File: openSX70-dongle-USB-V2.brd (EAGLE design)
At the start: 20 x 45 mm, 25 parts, among them J1 687106183722, J2 SJ-3523-SMT-TR, U1 FT232RLSSOP

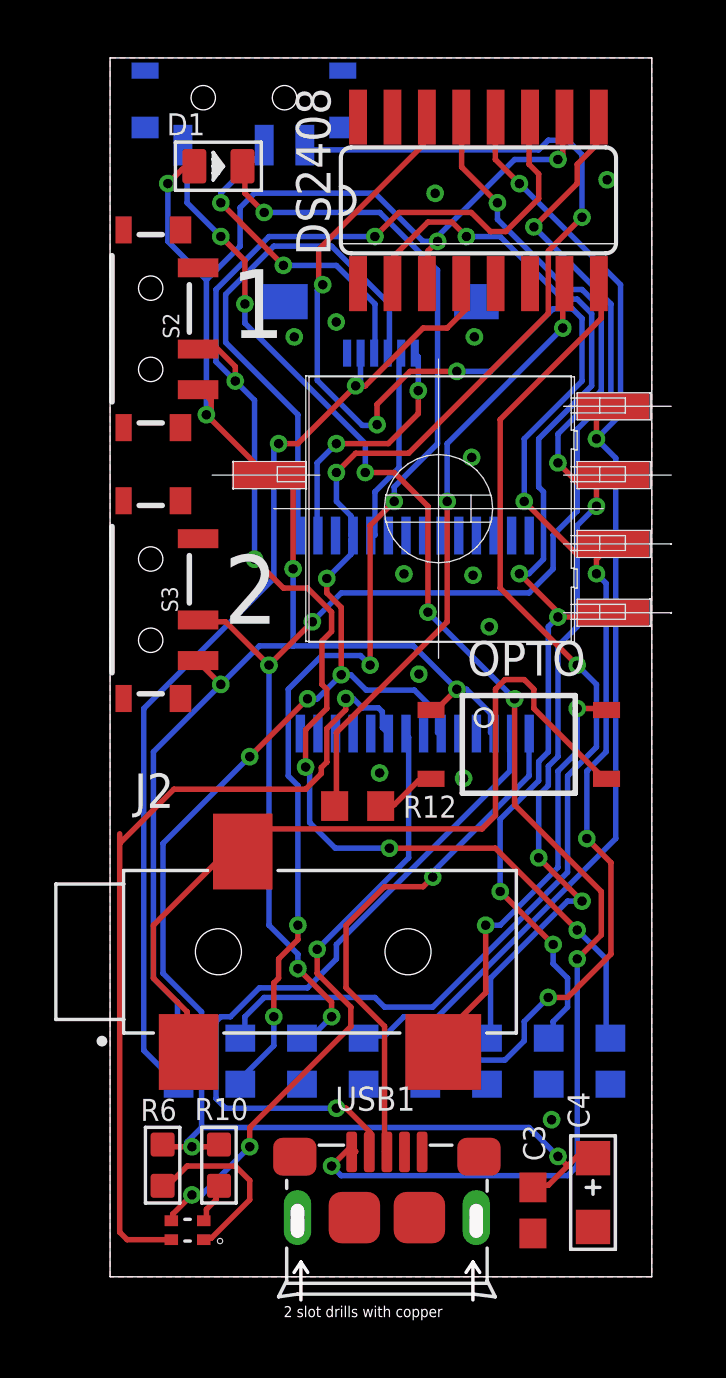
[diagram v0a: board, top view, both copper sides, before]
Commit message: fixed dual led footprint
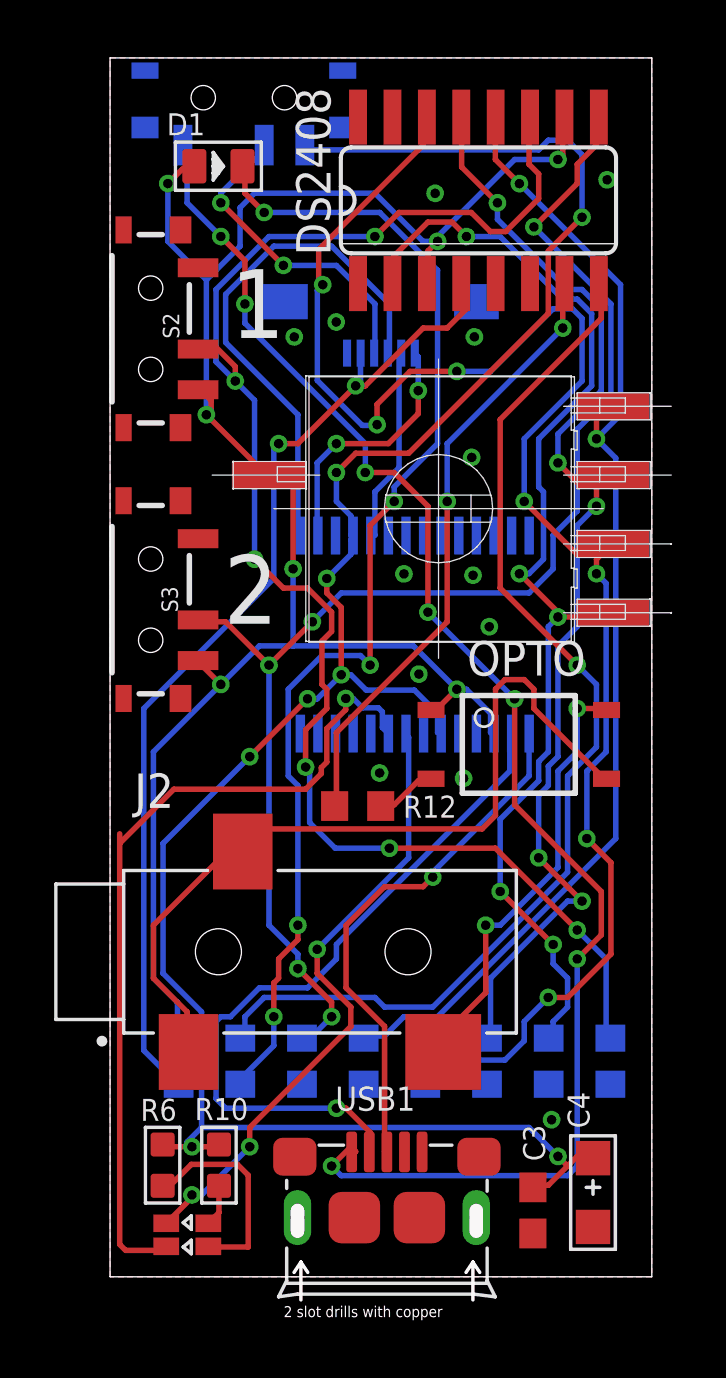
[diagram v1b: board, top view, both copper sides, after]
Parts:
- removed U$1: DUAL-LED-0603-BIS, _openSX70:LED_APHB1608SYKSURKC
- added U$5: DUOLED-PROPER-LTST-C195KGJRKT, _openSX70:LTST-BILED-15X16
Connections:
- net N$14: now also R6.1, U$5.P$1; no longer R10.1, U$1.3
- net N$9: now also R10.1, U$5.P$2; no longer R6.1, U$1.1
- net RXLED: now also U$5.P$4; no longer U$1.4
- net TXLED: now also U$5.P$3; no longer U$1.2
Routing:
- net N$14: track 1.52 -> 7.79 mm
- net N$9: track 6.96 -> 1.55 mm
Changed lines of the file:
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@@
 <attribute name="VALUE" x="7.347140625" y="9.23" size="1.27" layer="28" rot="MR270"/>
 </element>
-<element name="S1" library="SparkFun-Switches" library_urn="urn:adsk.eagle:library:535" package="SWITCH_SPST_SMD_A" package3d_urn="urn:adsk.eagle:package:40179/1" value="" x="4.94" y="43.53" rot="MR0">
+<element name="S1" library="SparkFun-Switches" package="SWITCH_SPST_SMD_A" value="" x="4.94" y="43.53" rot="MR0">
 <attribute name="NAME" x="4.878" y="43.033" size="0.6096" layer="26" font="vector" ratio="20" rot="MR180" align="bottom-center"/>
 <attribute name="PROD_ID" value="SWCH-10651" x="-23" y="-6" size="1.778" layer="28" rot="MR0" display="off"/>
@@
 <attribute name="VALUE" x="24.516" y="18.16" size="1.778" layer="27" ratio="10" rot="R90"/>
 </element>
-<element name="U$1" library="_openSX70" package="LED_APHB1608SYKSURKC" value="DUAL-LED-0603-BIS" x="2.86" y="1.72" rot="R180">
-<attribute name="NAME" x="4.71323125" y="0.81843125" size="0.81421875" layer="31" rot="R180"/>
-<attribute name="VALUE" x="4.863" y="3.42255" size="0.814021875" layer="27" rot="R180"/>
-</element>
 <element name="U1" library="SparkFun" package="SSOP28DB" value="FT232RLSSOP" x="11.25" y="23.71" rot="MR180">
 <attribute name="NAME" x="7.44" y="22.44" size="0.4064" layer="26" rot="MR180"/>
@@
 <attribute name="VALUE" x="5.14" y="0.415" size="0.889" layer="27" ratio="11" rot="R90"/>
 </element>
-<element name="S2" library="SparkFun-Switches" library_urn="urn:adsk.eagle:library:535" package="SWITCH_SPST_SMD_A" package3d_urn="urn:adsk.eagle:package:40179/1" value="" x="1.5" y="35" rot="R90">
+<element name="S2" library="SparkFun-Switches" package="SWITCH_SPST_SMD_A" value="" x="1.5" y="35" rot="R90">
 <attribute name="NAME" x="1.947" y="35.112" size="0.6096" layer="25" font="vector" ratio="20" rot="R270" align="bottom-center"/>
 <attribute name="PROD_ID" value="SWCH-10651" x="1.5" y="35" size="1.778" layer="27" rot="R90" display="off"/>
@@
 <attribute name="VALUE" x="0.103" y="35" size="0.6096" layer="27" font="vector" ratio="20" rot="R270" align="top-center"/>
 </element>
-<element name="S3" library="SparkFun-Switches" library_urn="urn:adsk.eagle:library:535" package="SWITCH_SPST_SMD_A" package3d_urn="urn:adsk.eagle:package:40179/1" value="" x="1.5" y="25" rot="R90">
+<element name="S3" library="SparkFun-Switches" package="SWITCH_SPST_SMD_A" value="" x="1.5" y="25" rot="R90">
 <attribute name="NAME" x="1.897" y="25.012" size="0.6096" layer="25" font="vector" ratio="20" rot="R270" align="bottom-center"/>
 <attribute name="PROD_ID" value="SWCH-10651" x="1.5" y="25" size="1.778" layer="27" rot="R90" display="off"/>
@@
 <attribute name="NAME" x="2.095" y="42.143" size="0.8128" layer="25" font="vector" ratio="11"/>
 <attribute name="VALUE" x="2.303" y="39.3125" size="0.635" layer="27" ratio="10"/>
+</element>
+<element name="U$5" library="_openSX70" package="LTST-BILED-15X16" value="DUOLED-PROPER-LTST-C195KGJRKT" x="2.85" y="1.55" rot="R270">
+<attribute name="AVAILABILITY" value="Unavailable" x="2.85" y="1.55" size="1.778" layer="27" rot="R270" display="off"/>
+<attribute name="DESCRIPTION" value=" Green/Red 130° Water Clear 35/25 mcd 2 V 0605 Surface Mount Bi-Color LED " x="2.85" y="1.55" size="1.778" layer="27" rot="R270" display="off"/>
+<attribute name="MF" value="Lite-On Inc." x="2.85" y="1.55" size="1.778" layer="27" rot="R270" display="off"/>
+<attribute name="MP" value="LTST-C195KGJRKT" x="2.85" y="1.55" size="1.778" layer="27" rot="R270" display="off"/>
+<attribute name="PACKAGE" value="0606 Lite-On" x="2.85" y="1.55" size="1.778" layer="27" rot="R270" display="off"/>
+<attribute name="PRICE" value="None" x="2.85" y="1.55" size="1.778" layer="27" rot="R270" display="off"/>
 </element>
 </elements>
@@
 <signal name="TXLED">
 <contactref element="U1" pad="23"/>
-<contactref element="U$1" pad="2"/>
-<wire x1="2.26" y1="1.37" x2="0.63" y2="1.37" width="0.2032" layer="1"/>
-<wire x1="0.63" y1="1.37" x2="0.3556" y2="1.6444" width="0.2032" layer="1"/>
-<wire x1="0.3556" y1="1.6444" x2="0.3556" y2="16" width="0.2032" layer="1"/>
+<wire x1="0.575" y1="0.975" x2="0.3556" y2="1.1944" width="0.2032" layer="1"/>
+<wire x1="0.3556" y1="1.1944" x2="0.3556" y2="16" width="0.2032" layer="1"/>
 <wire x1="0.3556" y1="16" x2="0.3556" y2="16.3556" width="0.2032" layer="1"/>
 <wire x1="10.275" y1="20.054" x2="10.053" y2="20.276" width="0.2032" layer="16"/>
@@
 <wire x1="8.7" y1="21.35" x2="8.7" y2="20.9377" width="0.2032" layer="1"/>
 <wire x1="8.7" y1="20.9377" x2="8.001" y2="20.2387" width="0.2032" layer="1"/>
-<wire x1="8.001" y1="19.001" x2="8" y2="19" width="0.2032" layer="1"/>
 <wire x1="8.001" y1="20.2387" x2="8.001" y2="19.001" width="0.2032" layer="1"/>
 <wire x1="2.3556" y1="18" x2="0.3556" y2="16" width="0.2032" layer="1"/>
-<wire x1="8" y1="19" x2="7.799" y2="18.799" width="0.2032" layer="1"/>
+<wire x1="8.001" y1="19.001" x2="7.799" y2="18.799" width="0.2032" layer="1"/>
 <wire x1="7.799" y1="18.799" x2="7.799" y2="18.578175" width="0.2032" layer="1"/>
 <wire x1="7.799" y1="18.578175" x2="7.220825" y2="18" width="0.2032" layer="1"/>
 <wire x1="7.220825" y1="18" x2="2.3556" y2="18" width="0.2032" layer="1"/>
+<contactref element="U$5" pad="P$3"/>
+<wire x1="1.9242" y1="0.975" x2="0.575" y2="0.975" width="0.2032" layer="1"/>
+<wire x1="2.0742" y1="1.125" x2="1.9242" y2="0.975" width="0.2032" layer="1"/>
 </signal>
 <signal name="RXLED">
 <contactref element="U1" pad="22"/>
-<contactref element="U$1" pad="4"/>
-<wire x1="2.3114" y1="2.3114" x2="2.3114" y2="2.1336" width="0.2032" layer="1"/>
-<wire x1="3.0226" y1="3.0226" x2="2.3114" y2="2.3114" width="0.2032" layer="1"/>
 <wire x1="3.3782" y1="3.0226" x2="3.0226" y2="3.0226" width="0.2032" layer="16"/>
 <wire x1="5.1562" y1="4.8006" x2="3.3782" y2="3.0226" width="0.2032" layer="16"/>
@@
 <wire x1="11.0236" y1="15.4686" x2="7.6454" y2="12.0904" width="0.2032" layer="16"/>
 <wire x1="11.0236" y1="19.9136" x2="11.0236" y2="15.4686" width="0.2032" layer="16"/>
-<wire x1="2.3114" y1="2.1336" x2="2.26" y2="2.07" width="0.2032" layer="1"/>
 <wire x1="11.0236" y1="19.9136" x2="10.925" y2="20.054" width="0.2032" layer="16"/>
 <via x="3.0226" y="3.0226" extent="1-16" drill="0.35"/>
 <via x="5.1562" y="4.8006" extent="1-16" drill="0.35"/>
 <via x="7.6454" y="12.0904" extent="1-16" drill="0.35"/>
+<contactref element="U$5" pad="P$4"/>
+<wire x1="3.0226" y1="3.0226" x2="3.0226" y2="2.9234" width="0.2032" layer="1"/>
+<wire x1="3.0226" y1="2.9234" x2="2.0742" y2="1.975" width="0.2032" layer="1"/>
 </signal>
 <signal name="TXO">
@@
 <via x="6.4008" y="37.338" extent="1-16" drill="0.35"/>
 <via x="4.0894" y="39.6494" extent="1-16" drill="0.35"/>
-</signal>
-<signal name="N$9">
-<contactref element="R6" pad="1"/>
-<contactref element="U$1" pad="1"/>
-<wire x1="3.7338" y1="1.4224" x2="3.556" y2="1.4224" width="0.2032" layer="1"/>
-<wire x1="5.1562" y1="2.8448" x2="3.7338" y2="1.4224" width="0.2032" layer="1"/>
-<wire x1="5.1562" y1="3.556" x2="5.1562" y2="2.8448" width="0.2032" layer="1"/>
-<wire x1="4.6228" y1="4.0894" x2="5.1562" y2="3.556" width="0.2032" layer="1"/>
-<wire x1="2.8448" y1="4.0894" x2="4.6228" y2="4.0894" width="0.2032" layer="1"/>
-<wire x1="1.9558" y1="3.2004" x2="2.8448" y2="4.0894" width="0.2032" layer="1"/>
-<wire x1="3.556" y1="1.4224" x2="3.46" y2="1.37" width="0.2032" layer="1"/>
-<wire x1="1.9558" y1="3.2004" x2="1.94" y2="3.358" width="0.2032" layer="1"/>
-</signal>
-<signal name="N$14">
-<contactref element="R10" pad="1"/>
-<contactref element="U$1" pad="3"/>
-<wire x1="3.556" y1="2.4892" x2="3.556" y2="2.1336" width="0.2032" layer="1"/>
-<wire x1="3.9116" y1="2.8448" x2="3.556" y2="2.4892" width="0.2032" layer="1"/>
-<wire x1="3.9116" y1="3.2004" x2="3.9116" y2="2.8448" width="0.2032" layer="1"/>
-<wire x1="3.556" y1="2.1336" x2="3.46" y2="2.07" width="0.2032" layer="1"/>
-<wire x1="3.9116" y1="3.2004" x2="4.02" y2="3.358" width="0.2032" layer="1"/>
 </signal>
 <signal name="VCC-USB">
@@
 <via x="5.6896" y="39.2938" extent="1-16" drill="0.35"/>
 </signal>
+<signal name="N$9">
+<contactref element="R10" pad="1"/>
+<contactref element="U$5" pad="P$2"/>
+<wire x1="4.02" y1="3.358" x2="4.02" y2="2.3692" width="0.2032" layer="1"/>
+<wire x1="4.02" y1="2.3692" x2="3.6258" y2="1.975" width="0.2032" layer="1"/>
+</signal>
+<signal name="N$14">
+<contactref element="R6" pad="1"/>
+<contactref element="U$5" pad="P$1"/>
+<wire x1="1.94" y1="3.358" x2="2.208" y2="3.358" width="0.2032" layer="1"/>
+<wire x1="3" y1="4.15" x2="4.7" y2="4.15" width="0.2032" layer="1"/>
+<wire x1="4.7" y1="4.15" x2="5.1" y2="3.75" width="0.2032" layer="1"/>
+<wire x1="5.1" y1="1.1" x2="3.6508" y2="1.1" width="0.2032" layer="1"/>
+<wire x1="3.6508" y1="1.1" x2="3.6258" y2="1.125" width="0.2032" layer="1"/>
+<wire x1="2.208" y1="3.358" x2="3" y2="4.15" width="0.2032" layer="1"/>
+<wire x1="5.1" y1="3.75" x2="5.1" y2="1.1" width="0.2032" layer="1"/>
+</signal>
 </signals>

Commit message: new origami design
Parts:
- added LED1: (no value), openSX70_PATHFINDER_V5.5-SEEED_20180522:LED3MM
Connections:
- net 3V3OUT: now also LED1.A
- net N$2: now also LED1.K
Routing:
- net 3V3OUT: track 71.8 -> 73.1 mm
- net N$2: track 44.3 -> 45.5 mm
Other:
- board text added: "A"
- board text added: "K"
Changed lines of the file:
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@@
 <layer number="14" name="Route14" color="22" fill="1" visible="no" active="no"/>
 <layer number="15" name="Route15" color="23" fill="1" visible="no" active="no"/>
-<layer number="16" name="Bottom" color="1" fill="1" visible="yes" active="yes"/>
+<layer number="16" name="Bottom" color="1" fill="1" visible="no" active="yes"/>
 <layer number="17" name="Pads" color="2" fill="1" visible="yes" active="yes"/>
 <layer number="18" name="Vias" color="2" fill="1" visible="yes" active="yes"/>
@@
 <layer number="20" name="Dimension" color="24" fill="1" visible="yes" active="yes"/>
 <layer number="21" name="tPlace" color="7" fill="1" visible="yes" active="yes"/>
-<layer number="22" name="bPlace" color="7" fill="1" visible="yes" active="yes"/>
+<layer number="22" name="bPlace" color="7" fill="1" visible="no" active="yes"/>
 <layer number="23" name="tOrigins" color="15" fill="1" visible="yes" active="yes"/>
-<layer number="24" name="bOrigins" color="15" fill="1" visible="yes" active="yes"/>
+<layer number="24" name="bOrigins" color="15" fill="1" visible="no" active="yes"/>
 <layer number="25" name="tNames" color="7" fill="1" visible="yes" active="yes"/>
-<layer number="26" name="bNames" color="7" fill="1" visible="yes" active="yes"/>
+<layer number="26" name="bNames" color="7" fill="1" visible="no" active="yes"/>
 <layer number="27" name="tValues" color="7" fill="1" visible="no" active="yes"/>
 <layer number="28" name="bValues" color="7" fill="1" visible="no" active="yes"/>
@@
 <layer number="38" name="bTest" color="7" fill="1" visible="no" active="yes"/>
 <layer number="39" name="tKeepout" color="4" fill="11" visible="yes" active="yes"/>
-<layer number="40" name="bKeepout" color="1" fill="11" visible="yes" active="yes"/>
+<layer number="40" name="bKeepout" color="1" fill="11" visible="no" active="yes"/>
 <layer number="41" name="tRestrict" color="4" fill="10" visible="yes" active="yes"/>
-<layer number="42" name="bRestrict" color="1" fill="10" visible="yes" active="yes"/>
+<layer number="42" name="bRestrict" color="1" fill="10" visible="no" active="yes"/>
 <layer number="43" name="vRestrict" color="2" fill="10" visible="no" active="yes"/>
-<layer number="44" name="Drills" color="7" fill="1" visible="yes" active="yes"/>
+<layer number="44" name="Drills" color="7" fill="1" visible="no" active="yes"/>
 <layer number="45" name="Holes" color="7" fill="1" visible="yes" active="yes"/>
 <layer number="46" name="Milling" color="3" fill="1" visible="no" active="yes"/>
@@
 <layer number="50" name="dxf" color="7" fill="1" visible="no" active="no"/>
 <layer number="51" name="tDocu" color="7" fill="1" visible="yes" active="yes"/>
-<layer number="52" name="bDocu" color="7" fill="1" visible="yes" active="yes"/>
+<layer number="52" name="bDocu" color="7" fill="1" visible="no" active="yes"/>
 <layer number="53" name="tGND_GNDA" color="7" fill="9" visible="no" active="no"/>
 <layer number="54" name="bGND_GNDA" color="1" fill="9" visible="no" active="no"/>
@@
 <text x="6.45" y="37.2" size="2.54" layer="21" font="vector" rot="R180">1</text>
 <text x="6.2" y="26.65" size="2.54" layer="21" font="vector" rot="R180">2</text>
-<dimension x1="0" y1="45" x2="20" y2="45" x3="10" y3="45" textsize="1.778" layer="1"/>
+<dimension x1="0" y1="45" x2="20" y2="45" x3="10" y3="48" textsize="1.778" layer="1"/>
+<dimension x1="20" y1="45" x2="20" y2="0" x3="27" y3="22.5" textsize="1.778" layer="1"/>
+<text x="1.15" y="41.15" size="0.8128" layer="25" font="vector" ratio="20">A</text>
+<text x="6.2" y="40.95" size="0.8128" layer="25" font="vector" ratio="20">K</text>
 </plain>
 <attributes>
@@
 <element name="D1" library="Seeed-LED-2016" package="LED-0805" value="YELLOW-0805" x="4" y="41">
 <attribute name="MPN" value="17-215UYC/S530-A3/TR8" x="4" y="41" size="1.778" layer="27" display="off"/>
-<attribute name="NAME" x="2.095" y="42.143" size="0.8128" layer="25" font="vector" ratio="11"/>
+<attribute name="NAME" x="0.695" y="43.593" size="0.8128" layer="25" font="vector" ratio="11"/>
 <attribute name="VALUE" x="2.303" y="39.3125" size="0.635" layer="27" ratio="10"/>
 </element>
@@
 <attribute name="PACKAGE" value="0606 Lite-On" x="2.85" y="1.55" size="1.778" layer="27" rot="R270" display="off"/>
 <attribute name="PRICE" value="None" x="2.85" y="1.55" size="1.778" layer="27" rot="R270" display="off"/>
+</element>
+<element name="LED1" library="openSX70_PATHFINDER_V5.5-SEEED_20180522" package="LED3MM" value="" x="4" y="42">
+<attribute name="VALUE" x="7.2004" y="40.1966" size="1.27" layer="27" ratio="10"/>
 </element>
 </elements>
@@
 <via x="16.5354" y="41.2496" extent="1-16" drill="0.35"/>
 <via x="6.7564" y="26.1366" extent="1-16" drill="0.35"/>
+<contactref element="LED1" pad="A"/>
+<wire x1="2.73" y1="42" x2="2.73" y2="41.1866" width="0.2032" layer="1"/>
+<wire x1="2.73" y1="41.1866" x2="3.0226" y2="40.894" width="0.2032" layer="1"/>
 </signal>
 <signal name="N$1">
@@
 <wire x1="6.0452" y1="8.5344" x2="4.9784" y2="7.4676" width="0.2032" layer="16"/>
 <wire x1="6.0452" y1="9.6012" x2="6.0452" y2="8.5344" width="0.2032" layer="16"/>
-<wire x1="6.0452" y1="10.8458" x2="6.0452" y2="9.6012" width="0.2032" layer="1"/>
-<wire x1="6.223" y1="11.0236" x2="6.0452" y2="10.8458" width="0.2032" layer="1"/>
-<wire x1="6.223" y1="11.7348" x2="6.223" y2="11.0236" width="0.2032" layer="1"/>
-<wire x1="6.9342" y1="12.446" x2="6.223" y2="11.7348" width="0.2032" layer="1"/>
+<wire x1="6.0452" y1="11.557" x2="6.0452" y2="9.6012" width="0.2032" layer="1"/>
+<wire x1="6.9342" y1="12.446" x2="6.0452" y2="11.557" width="0.2032" layer="1"/>
 <wire x1="6.9342" y1="12.9794" x2="6.9342" y2="12.446" width="0.2032" layer="1"/>
 <wire x1="6.9342" y1="18.1356" x2="6.9342" y2="12.9794" width="0.2032" layer="16"/>
@@
 <via x="10.4902" y="28.6258" extent="1-16" drill="0.35"/>
 <via x="5.6896" y="39.2938" extent="1-16" drill="0.35"/>
+<contactref element="LED1" pad="K"/>
+<wire x1="5.27" y1="42" x2="5.27" y2="41.381" width="0.2032" layer="1"/>
+<wire x1="5.27" y1="41.381" x2="4.889" y2="41" width="0.2032" layer="1"/>
 </signal>
 <signal name="N$9">
